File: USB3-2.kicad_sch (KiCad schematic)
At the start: 45 parts, among them J4 Conn_USB-C_WE_632723300011, Q3 PJE138K, U12 AP22615A_TSOT26, U14 TPD4E05U06QDQARQ1, U15 TPD4E05U06QDQARQ1, U16 TPD4E05U06QDQARQ1, U2 HD3SS3220RNH

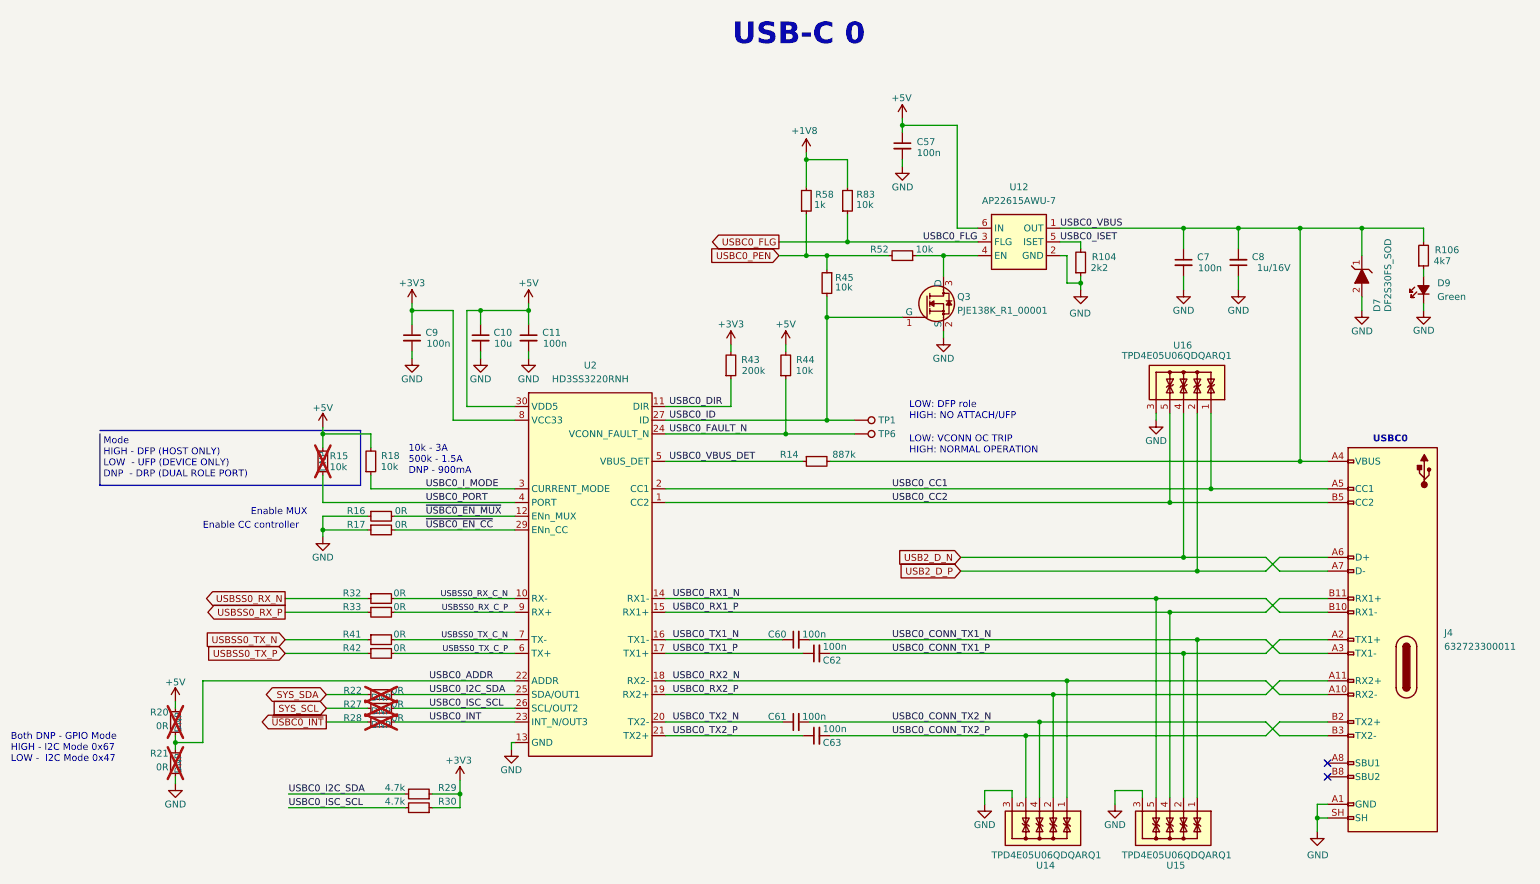
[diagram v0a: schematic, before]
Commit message: Schematic Cleanup, Complete routing
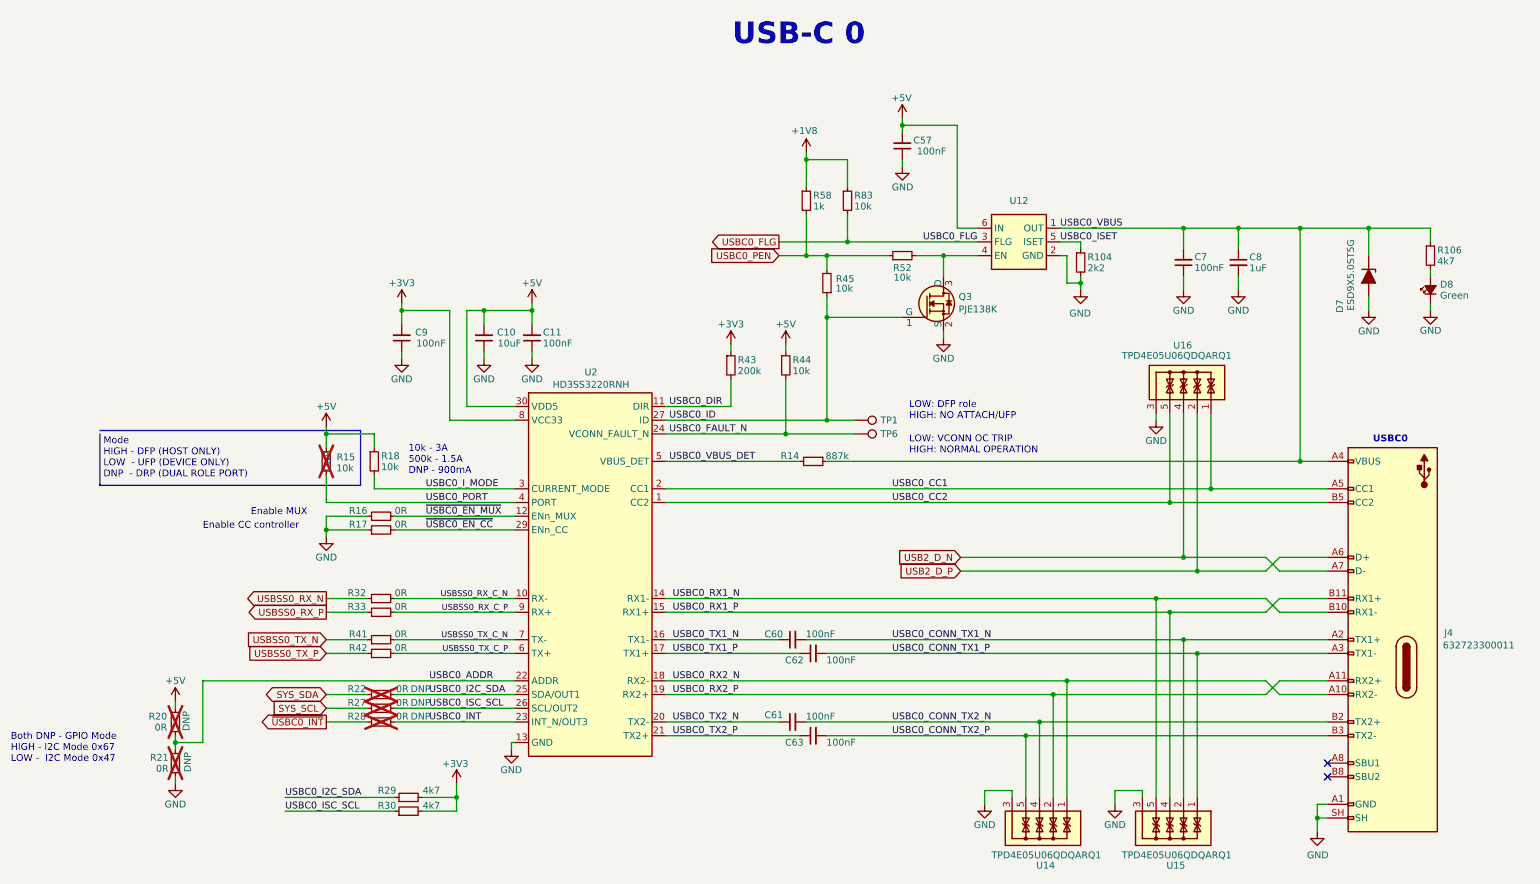
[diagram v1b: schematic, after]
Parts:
- C10: value C_10u_0603 -> 10uF; symbol antmicroCapacitors0603:C_10u_0603 -> Device:C_Small
- C11, C57, C7, C9: value C_100n_0603 -> 100nF; symbol antmicroCapacitors0402:C_100n_0402 -> Device:C_Small
- C60, C61, C62, C63: value C_100n_0402 -> 100nF; symbol antmicroCapacitors0402:C_100n_0402 -> Device:C_Small
- C8: value C_1u_16V_0603 -> 1uF; symbol antmicroCapacitors0402:C_1u_16V_0402 -> Device:C_Small
- D7: value DF2S30FS_SOD -> ESD9X5.0ST5G; symbol antmicroTVSDiodes:DF2S30FS_SOD -> Device:D_Zener_Filled
- D8: renamed from D9; symbol antmicroLEDIndicationDiscrete:LED_G_0603_LTST-C190GKT -> Device:LED_Small_Filled
- J4: value Conn_USB-C_WE_632723300011 -> 632723300011; symbol antmicroUSBConnectors:USB-C_WE_632723300011 -> JetsonCarrier:USB-C_WE_632723300011
- Q3: symbol antmicroTransistorsFETsMOSFETsSingle:PJE138K -> JetsonCarrier:PJE138K
- R104: value R_2k2_0603 -> 2k2; symbol antmicroResistors0402:R_2k2_0402 -> Device:R_Small
- R106: value R_4k7_0603 -> 4k7; symbol antmicroResistors0402:R_4k7_0402 -> Device:R_Small
- R14: value R_887k_0603 -> 887k; symbol antmicroResistors0402:R_887k_0402 -> Device:R_Small
- R15: value R_10k_0603 -> 10k; symbol antmicroResistors0402:R_10k_0402 -> Device:R_Small; now in the parts list
- R16, R17, R32, R33, R41, R42: value R_0R_0402 -> 0R; symbol antmicroResistors0402:R_0R_0402 -> Device:R_Small
- R18, R44, R45, R52, R83: value R_10k_0603 -> 10k; symbol antmicroResistors0402:R_10k_0402 -> Device:R_Small
- R20, R21, R22, R27, R28: value R_0R_0402 -> 0R; symbol antmicroResistors0402:R_0R_0402 -> Device:R_Small; now in the parts list
- R29, R30: value R_4k7_0603 -> 4k7; symbol antmicroResistors0402:R_200k_0402 -> Device:R_Small; Val 4.7k -> 4k7
- R43: value R_200k_0603 -> 200k; symbol antmicroResistors0402:R_200k_0402 -> Device:R_Small
- R58: value R_10k_0603 -> 1k; symbol antmicroResistors0402:R_10k_0402 -> Device:R_Small
- TP1, TP6: symbol antmicroTestPoints:TP_0.75mm_SMD -> Connector:TestPoint
- U12: symbol antmicroPMICPowerDistributionSwitchesLoadDrivers:AP22615A_TSOT26 -> JetsonCarrier:AP22615A_TSOT26
- U14, U15, U16: symbol antmicroTVSDiodes:TPD4E05U06QDQARQ1 -> JetsonCarrier:TPD4E05U06QDQARQ1
- U2: symbol antmicroInterfaceControllers:HD3SS3220RNH -> JetsonCarrier:HD3SS3220RNH
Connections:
- net +1V8: now also R58.1, R83.1; no longer R58.2, R83.2
- net +3V3: now also C9.2, R29.2, R30.2, R43.1; no longer C9.1, R29.1, R30.1, R43.2
- net +5V: now also C10.2, C11.2, C57.2, R15.2, R18.1, R44.1; no longer C10.1, C11.1, C57.1, R15.1, R18.2, R44.2
- net GND: now also C10.1, C11.1, C57.1, C7.1, C8.2, C9.1, R104.2; no longer C10.2, C11.2, C57.2, C7.2, C8.1, C9.2, R104.1
- net USBC0_CONN_TX1_N: now also J4.A2 (TX1+), U15.2, U15.9; no longer J4.A3 (TX1-), U15.1, U15.10
- net USBC0_CONN_TX1_P: now also J4.A3 (TX1-), U15.1, U15.10; no longer J4.A2 (TX1+), U15.2, U15.9
- net USBC0_CONN_TX2_N: now also J4.B2 (TX2+); no longer J4.B3 (TX2-)
- net USBC0_CONN_TX2_P: now also J4.B3 (TX2-); no longer J4.B2 (TX2+)
- net USBC0_DIR: now also R43.2; no longer R43.1
- net USBC0_FAULT_N: now also R44.2; no longer R44.1
- net USBC0_FLG: now also R83.2; no longer R83.1
- net USBC0_I2C_SDA: now also R29.1; no longer R29.2
- net USBC0_ID: now also R45.1; no longer R45.2
- net USBC0_ISC_SCL: now also R30.1; no longer R30.2
- net USBC0_ISET: now also R104.1; no longer R104.2
- net USBC0_I_MODE: now also R18.2; no longer R18.1
- net USBC0_PEN: now also R45.2, R52.1, R58.2; no longer R45.1, R52.2, R58.1
- net USBC0_PORT: now also R15.1; no longer R15.2
- net USBC0_VBUS: now also C7.2, C8.1, R106.1, R14.1; no longer C7.1, C8.2, R106.2, R14.2
- net USBC0_VBUS_DET: now also R14.2; no longer R14.1
- net at Q3.3 (D), U12.4 (EN): now also R52.2; no longer R52.1
- net at D8.2 (A): now also R106.2; no longer R106.1
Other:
- moved on the sheet: C10, C11, C57, C60, C61, C62, C63, C7, C8, C9, R104, R106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
